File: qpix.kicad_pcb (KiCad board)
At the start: 4 copper layers, 82.6 x 92.8 mm, 109 parts, among them J1 Conn_01x40, J10 VC, J11 Conn_Coaxial_Power, J13 DigReset, J2 Conn_01x09, J3 Conn_02x03, J4 Conn_02x03, J5 SPI, J6 Conn_02x03, J7 Conn_Coaxial, J8 Conn_02x03, J9 Conn_Coaxial_Power, Q1 Q_NMOS_GSD, Q2 Q_NMOS_GSD, Q3 Q_NMOS_GSD, Q4 Q_NMOS_GSD, U1 qpix_digital, U2 TPS73101DBV, U3 9DMV0141AKILF, U4 DS90C401M_NOPB

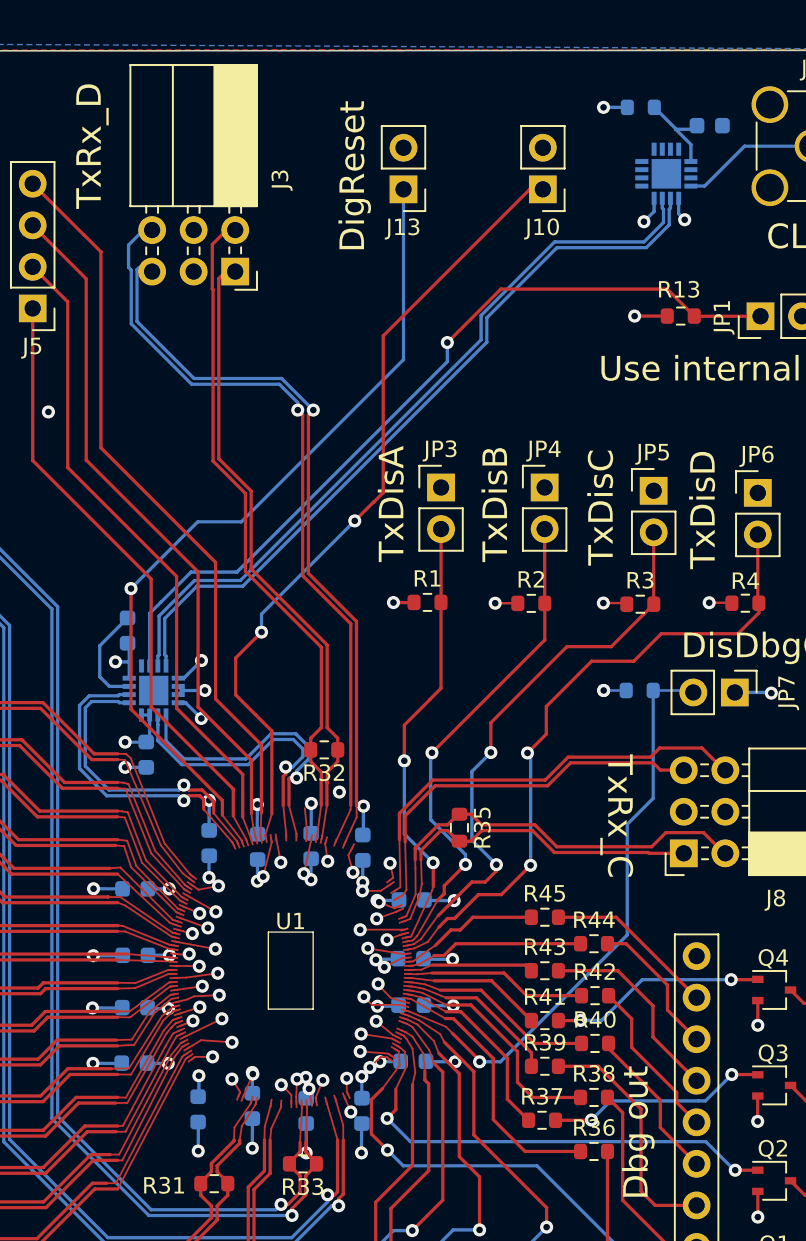
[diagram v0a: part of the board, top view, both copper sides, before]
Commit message: move some vias a little, re-flood copper areas
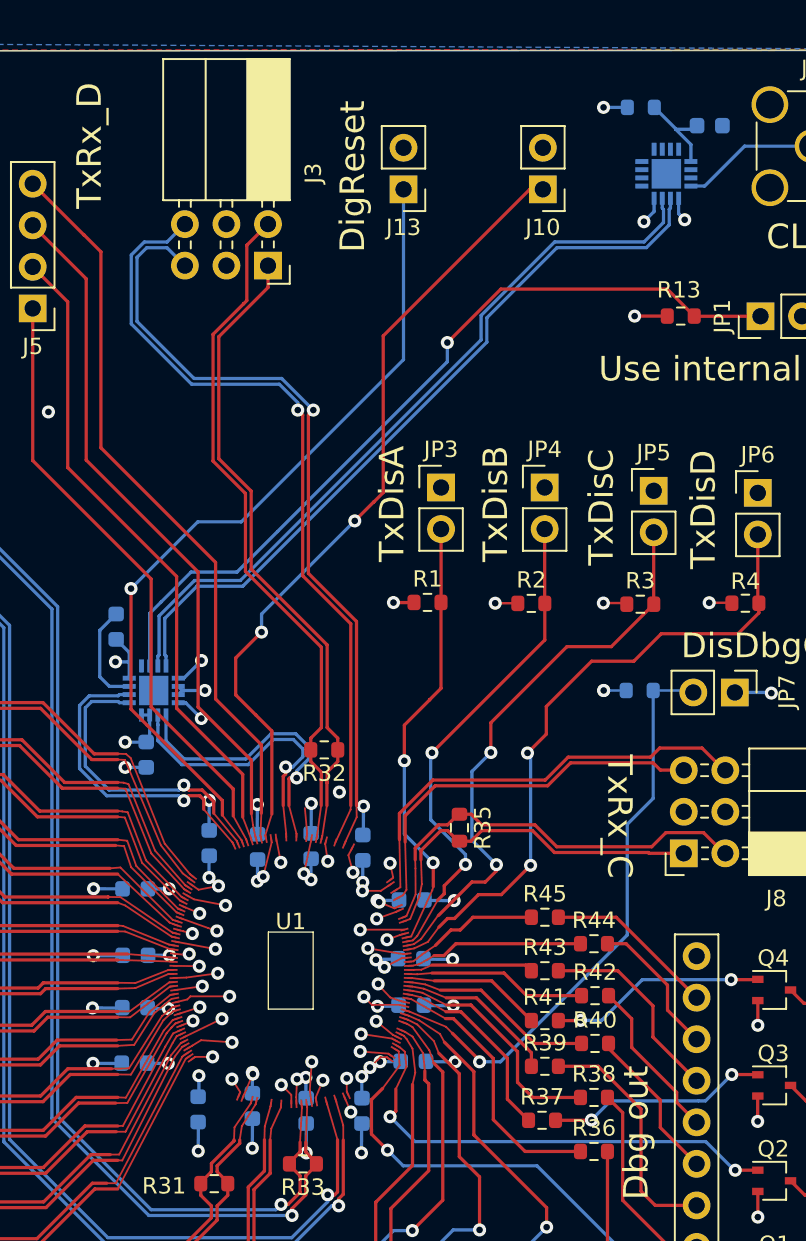
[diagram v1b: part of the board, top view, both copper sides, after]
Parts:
- moved J3 2.04 mm to (139.3, 62.6)
- moved C19 0.74 mm to (130.0, 84.7)
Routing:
- net /DataoutD_P: track 45.0 -> 48.7 mm
- net VDD: track 84.6 -> 87.4 mm
- net /DataoutD_N: track 47.6 -> 48.9 mm
- net GND: track 108.8 -> 109.8 mm
- net /DatainD_P: track 39.0 -> 39.7 mm
- net /DatainD_N: track 41.7 -> 42.3 mm

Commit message: set solder mask expansion 0.15 mm, and 0.3mm for qpix-digital footprint
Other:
- rule pad_to_mask_clearance: 0 -> 0.15
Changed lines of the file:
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@@
       (dielectric_constraints no)
     )
-    (pad_to_mask_clearance 0)
+    (pad_to_mask_clearance 0.15)
     (pcbplotparams
       (layerselection 0x00010fc_ffffffff)
@@
     (property "Sheetfile" "qpix.kicad_sch")
     (property "Sheetname" "")
-    (solder_mask_margin 0.15)
+    (solder_mask_margin 0.3)
     (attr smd)
     (fp_text reference "U1" (at 0 -3) (layer "F.SilkS")

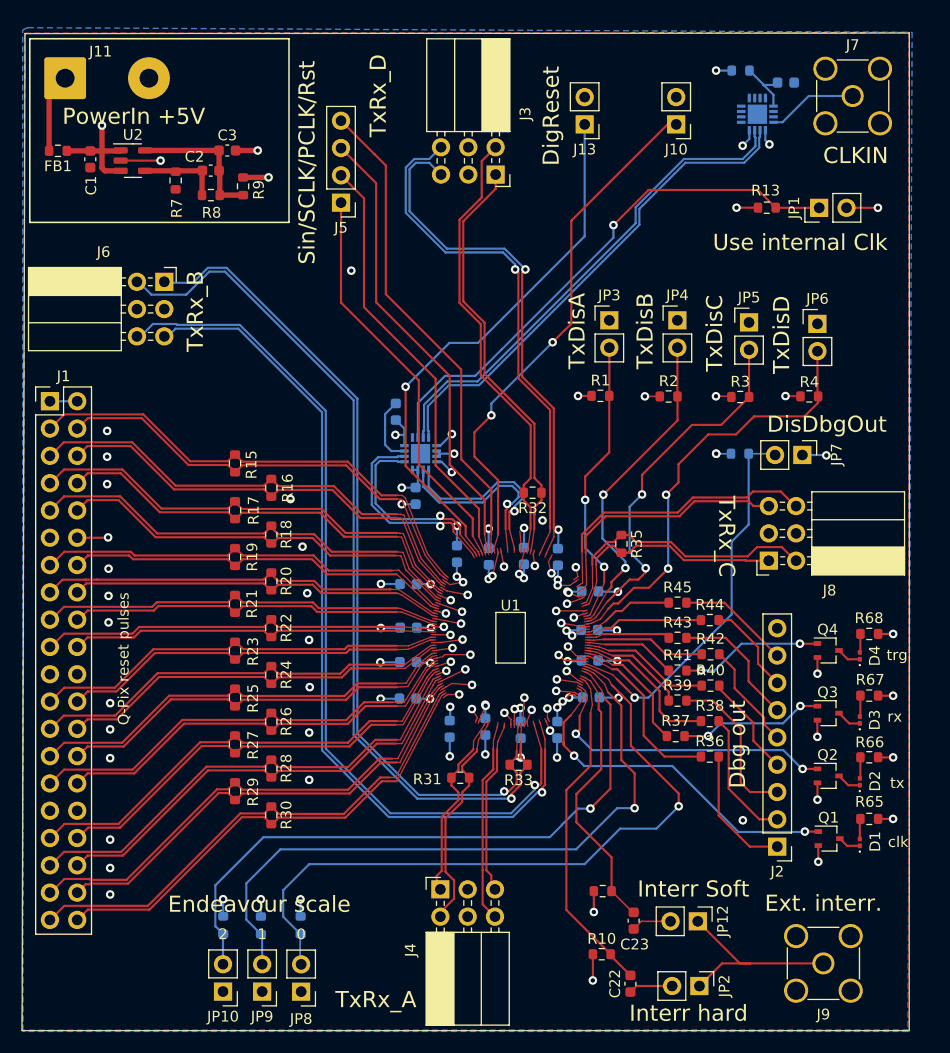
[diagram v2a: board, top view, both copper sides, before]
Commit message: add part values for missed ones
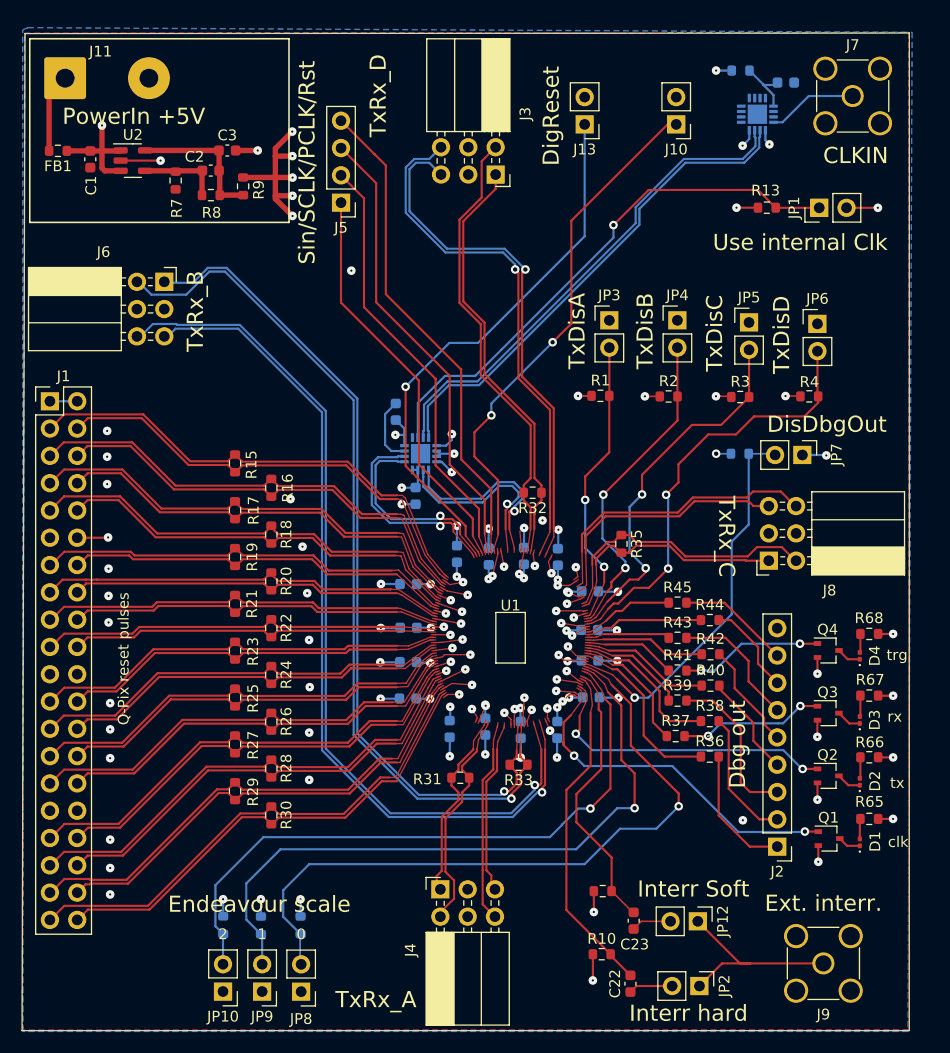
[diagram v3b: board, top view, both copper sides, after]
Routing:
- net VDD: track 87.4 -> 102.0 mm, vias 53 -> 56

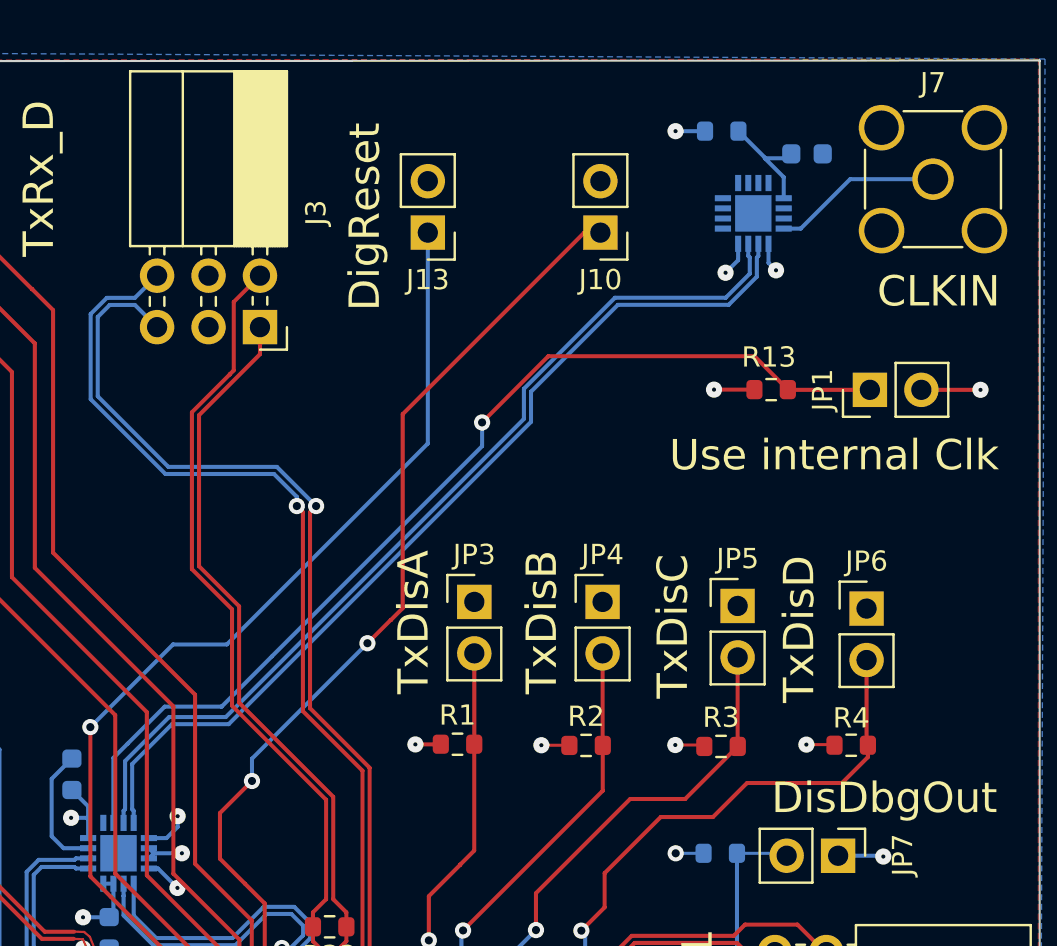
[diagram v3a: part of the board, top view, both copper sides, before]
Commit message: fix external clock input
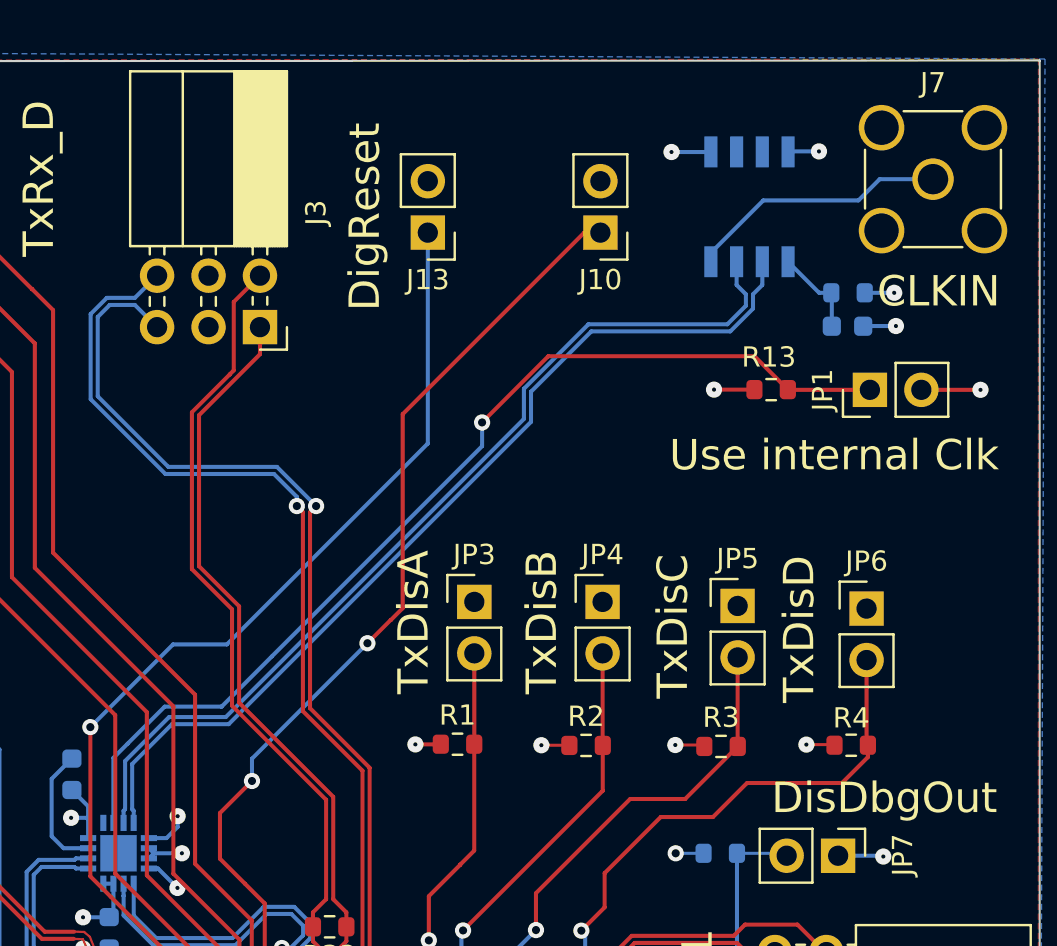
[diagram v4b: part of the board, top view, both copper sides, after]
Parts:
- C1, C3: value C -> 10uF
- C10, C8: value C -> 220 nF
- C11, C9: value C -> 2 nF
- C12, C24: value C -> 22uF
- C17, C18: value C -> 2nF
- C19, C20, C21: value C -> 0.1uF
- C2: value C -> 15pF
- C22, C23: value C -> 100nF
- C4, C5: value C -> 22 uF
- C6, C7: value C -> 2.2 uF
- FB1: value FerriteBead -> LQM18FN2R2M00D
- Q1, Q2, Q3, Q4: value Q_NMOS_GSD -> AO7400
- R1, R11, R12, R2, R3, R4, R5: value R_US -> 10k
- R10, R13, R14, R34: value R_Small_US -> 22k
- R6: value (none) -> 10k
- R7: value R_US -> 56.2k
- R8: value R_US -> 28.0k
- R9: value 1 -> 0
- U4: footprint 9DMV0141AKILF:QFN50P300X300X100-17N -> DS90C401M:SOIC127P600X175-8N
- moved R34 10.1 mm to (168.3, 60.9), turned to 0 degrees
- moved C21 8.74 mm to (168.3, 62.5)
- moved U4 0.38 mm to (163.5, 56.6), turned to 90 degrees
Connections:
- net Net-(J7-In) renamed /clkmux/CLK_DIN
- U4 pad 2: unconnected-(U4-DO1--Pad2) -> /clkmux/DO-
- U4 pad 3: unconnected-(U4-DO1+-Pad3) -> /clkmux/DO+
- U4 pad 6: /clkmux/DO- -> unconnected-(U4-DO2--Pad6)
- U4 pad 7: /clkmux/DO+ -> unconnected-(U4-DO2+-Pad7)
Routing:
- net /clkmux/CLK_DIN: track 8.38 -> 12.9 mm
- net GND: track 110.0 -> 112.0 mm, vias 75 -> 76
- net Net-(U4-VCC): track 5.63 -> 4.43 mm

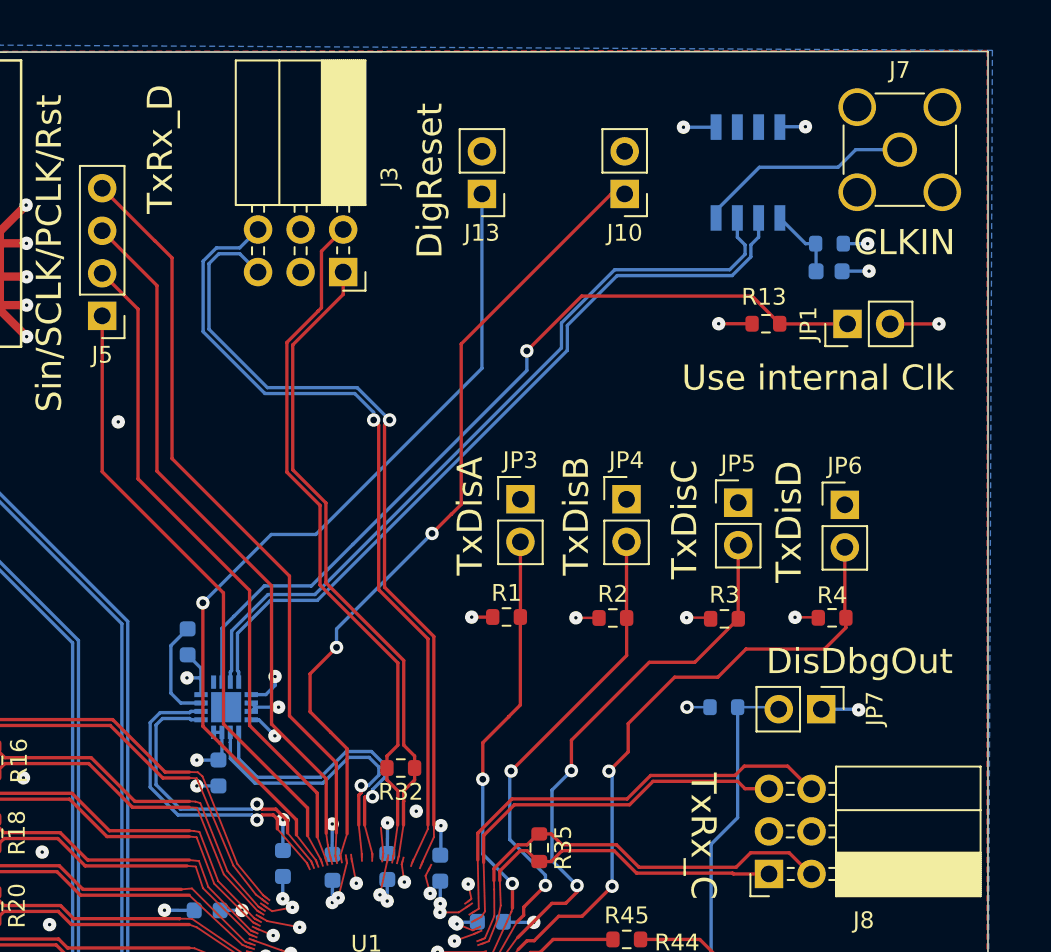
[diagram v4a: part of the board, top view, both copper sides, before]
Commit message: clk select related components moved to the top layer
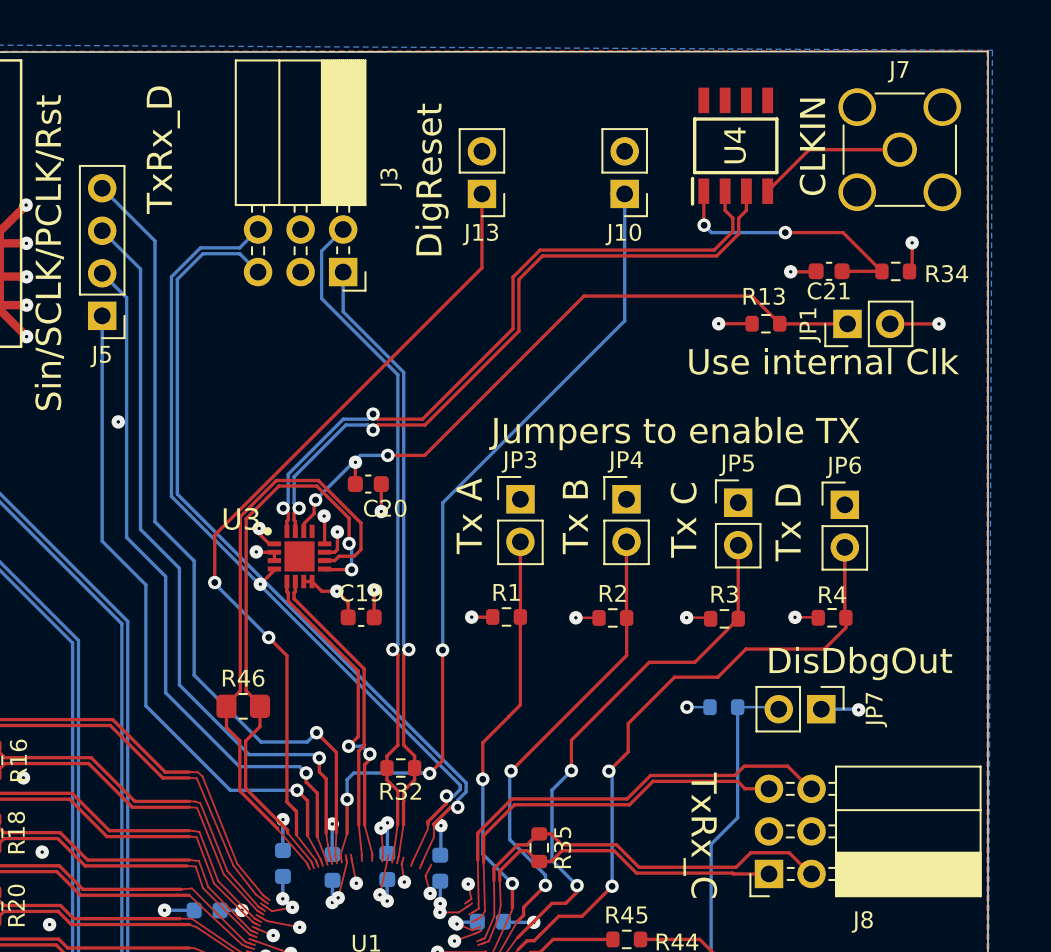
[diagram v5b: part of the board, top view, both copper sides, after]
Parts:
- added R46: NC, Resistor_SMD:R_0805_2012Metric_Pad1.20x1.40mm_HandSolder, F.Cu at (133.3, 88.5)
- C19, C20, C21, R34, U3, U4: moved to F.Cu
- moved C20 19.4 mm to (140.8, 75.2), turned to 0 degrees
- moved C19 10.5 mm to (140.4, 83.2), turned to 0 degrees
- moved U3 10.0 mm to (136.7, 79.6), turned to 0 degrees
- moved R34 4.29 mm to (172.3, 62.5)
- moved U4 1.75 mm to (162.8, 55.0)
- turned C21 to 180 degrees
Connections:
- net /clkmux/SEL_AB renamed /clkmux/SEL_CLK
- net Net-(J10-Pin_1) renamed /VC
- net Net-(J13-Pin_1) renamed /DigReset
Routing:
- net CLKDIGIINN: track 19.3 -> 36.3 mm, vias 1 -> 0
- net CLKDIGIINP: track 18.6 -> 35.4 mm, vias 1 -> 2
- net Net-(U4-VCC): track 4.43 -> 16.2 mm, vias 0 -> 2
- net /clkmux/SEL_CLK: track 50.1 -> 39.6 mm, vias 1 -> 2
- net GND: track 112.0 -> 104.7 mm
- net /clkmux/DO-: track 46.3 -> 40.9 mm, vias 0 -> 2
- net /clkmux/DO+: track 46.3 -> 40.9 mm, vias 0 -> 2
- net /clkmux/CLK_DIN: track 12.9 -> 8.91 mm
- net /SR_reset: track 45.9 -> 48.6 mm, vias 0 -> 1
- net /PCLK: track 43.2 -> 45.5 mm, vias 0 -> 1
- net /Sin: track 37.9 -> 40.3 mm, vias 0 -> 1
- net /DatainD_P: track 39.7 -> 37.4 mm, vias 0 -> 1
- net /DigReset: track 51.2 -> 49.0 mm, vias 1 -> 2
- net /SCLK: track 40.5 -> 42.6 mm, vias 0 -> 1
- net CLKOUTP: track 18.1 -> 19.7 mm, vias 1 -> 2
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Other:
- rule pad_to_mask_clearance: 0.15 -> -0.5
- board text added: "Jumpers to enable TX"
- board text added: "Tx A"
- board text added: "Tx B"
- board text added: "Tx C"
- board text added: "Tx D"
- board text removed: "TxDisA"
- board text removed: "TxDisB"
- board text removed: "TxDisC"
- board text removed: "TxDisD"
